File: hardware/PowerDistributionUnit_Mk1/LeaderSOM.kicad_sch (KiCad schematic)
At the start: 14 parts, among them J10 Logic Analyzer, J11 Logic Analyzer, J12 Logic Analyzer, U1 LeaderSOM

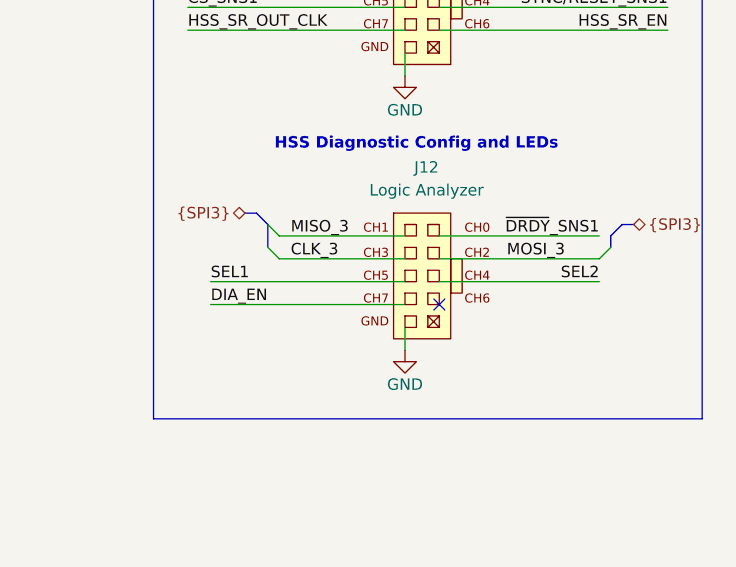
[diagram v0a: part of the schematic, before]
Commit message: add routing for DIA and HSS SR connections
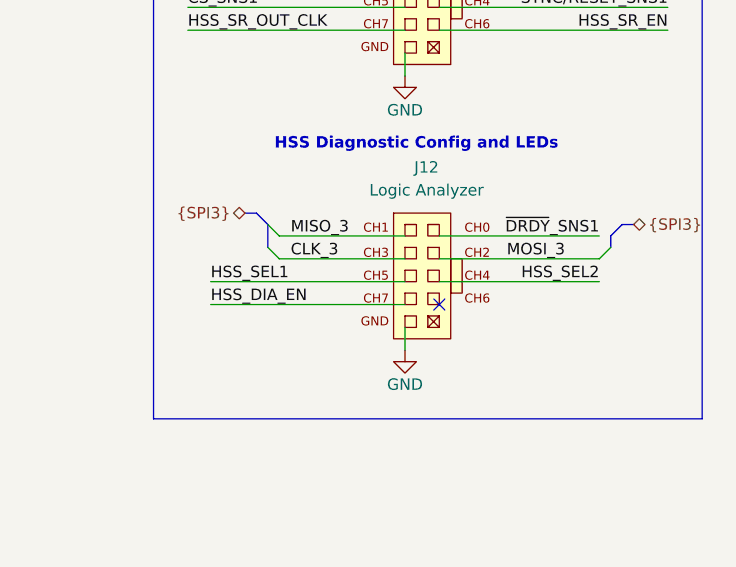
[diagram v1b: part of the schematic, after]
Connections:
- net DIA_EN is gone; now on net HSS_DIA_EN: J12.3 (CH7)
- net SEL1 is gone; now on net HSS_SEL1: J12.5 (CH5)
- net SEL2 is gone; now on net HSS_SEL2: J12.6 (CH4)
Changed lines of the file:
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@@
 		)
 	)
-	(label "SEL1"
+	(label "HSS_SEL1"
 		(at 218.44 113.03 0)
 		(effects
@@
 		)
 	)
-	(label "SEL2"
+	(label "HSS_SEL2"
 		(at 261.62 113.03 180)
 		(effects
@@
 		)
 	)
-	(label "DIA_EN"
+	(label "HSS_DIA_EN"
 		(at 218.44 115.57 0)
 		(effects

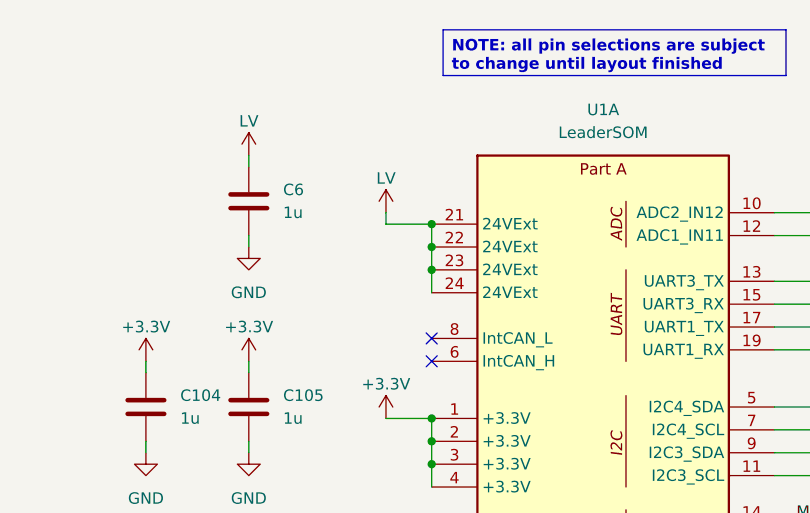
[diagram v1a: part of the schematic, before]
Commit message: all connections routed
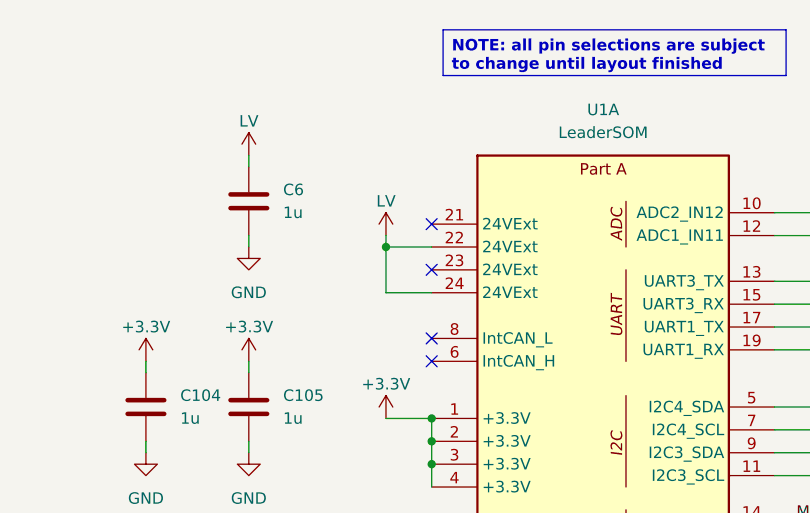
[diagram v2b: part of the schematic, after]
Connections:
- net LV: no longer U1.21 (24VExt), U1.23 (24VExt)
- no-connect marks 5 -> 7
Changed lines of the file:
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@@
 	)
 	(junction
-		(at 119.38 50.8)
+		(at 114.3 48.26)
 		(diameter 0)
 		(color 0 0 0 0)
@@
 	)
 	(junction
-		(at 119.38 48.26)
-		(diameter 0)
-		(color 0 0 0 0)
-	)
-	(junction
-		(at 119.38 45.72)
-		(diameter 0)
-		(color 0 0 0 0)
-	)
-	(junction
 		(at 119.38 69.85)
 		(diameter 0)
@@
 	)
 	(no_connect
+		(at 119.38 50.8)
+	)
+	(no_connect
+		(at 119.38 45.72)
+	)
+	(no_connect
 		(at 45.72 132.08)
 	)
@@
 	(wire
 		(pts
-			(xy 119.38 45.72) (xy 119.38 48.26)
-		)
-		(stroke
-			(width 0)
-			(type default)
-		)
-	)
-	(wire
-		(pts
 			(xy 55.88 142.24) (xy 55.88 143.51)
 		)
@@
 	(wire
 		(pts
-			(xy 226.06 107.95) (xy 240.03 107.95)
+			(xy 114.3 46.99) (xy 114.3 48.26)
 		)
 		(stroke
@@
 	(wire
 		(pts
-			(xy 157.48 146.05) (xy 167.64 146.05)
+			(xy 226.06 107.95) (xy 240.03 107.95)
 		)
 		(stroke
@@
 	(wire
 		(pts
-			(xy 157.48 125.73) (xy 165.1 125.73)
+			(xy 157.48 146.05) (xy 167.64 146.05)
 		)
 		(stroke
@@
 	(wire
 		(pts
-			(xy 226.06 77.47) (xy 240.03 77.47)
+			(xy 157.48 125.73) (xy 165.1 125.73)
 		)
 		(stroke
@@
 	(wire
 		(pts
-			(xy 87.63 69.85) (xy 87.63 71.12)
+			(xy 226.06 77.47) (xy 240.03 77.47)
 		)
 		(stroke
@@
 		)
 	)
-	(bus
+	(wire
 		(pts
-			(xy 168.91 77.47) (xy 170.18 76.2)
+			(xy 87.63 69.85) (xy 87.63 71.12)
 		)
 		(stroke
@@
 		)
 	)
-	(wire
+	(bus
 		(pts
-			(xy 119.38 50.8) (xy 119.38 53.34)
+			(xy 168.91 77.47) (xy 170.18 76.2)
 		)
 		(stroke
@@
 		)
 	)
-	(wire
+	(bus
 		(pts
-			(xy 119.38 48.26) (xy 119.38 50.8)
+			(xy 265.43 106.68) (xy 264.16 106.68)
 		)
 		(stroke
@@
 		)
 	)
-	(bus
+	(wire
 		(pts
-			(xy 265.43 106.68) (xy 264.16 106.68)
+			(xy 116.84 144.78) (xy 116.84 147.32)
 		)
 		(stroke
@@
 	(wire
 		(pts
-			(xy 116.84 144.78) (xy 116.84 147.32)
+			(xy 215.9 54.61) (xy 240.03 54.61)
 		)
 		(stroke
@@
 	(wire
 		(pts
-			(xy 215.9 54.61) (xy 240.03 54.61)
+			(xy 114.3 53.34) (xy 119.38 53.34)
 		)
 		(stroke
@@
 	(wire
 		(pts
+			(xy 114.3 48.26) (xy 114.3 53.34)
+		)
+		(stroke
+			(width 0)
+			(type default)
+		)
+	)
+	(wire
+		(pts
 			(xy 240.03 118.11) (xy 240.03 120.65)
 		)
@@
 	(wire
 		(pts
-			(xy 114.3 44.45) (xy 114.3 45.72)
-		)
-		(stroke
-			(width 0)
-			(type default)
-		)
-	)
-	(wire
-		(pts
 			(xy 243.84 77.47) (xy 260.35 77.47)
 		)
@@
 	(wire
 		(pts
-			(xy 114.3 45.72) (xy 119.38 45.72)
+			(xy 114.3 48.26) (xy 119.38 48.26)
 		)
 		(stroke
@@
 	(symbol
 		(lib_id "power:+24V")
-		(at 114.3 44.45 0)
+		(at 114.3 46.99 0)
 		(unit 1)
 		(exclude_from_sim no)
@@
 		(dnp no)
 		(property "Reference" "#PWR017"
-			(at 114.3 48.26 0)
+			(at 114.3 50.8 0)
 			(effects
 				(font
@@
 		)
 		(property "Value" "LV"
-			(at 114.3 40.64 0)
+			(at 114.3 43.18 0)
 			(effects
 				(font
@@
 		)
 		(property "Footprint" ""
-			(at 114.3 44.45 0)
+			(at 114.3 46.99 0)
 			(effects
 				(font
@@
 		)
 		(property "Datasheet" ""
-			(at 114.3 44.45 0)
+			(at 114.3 46.99 0)
 			(effects
 				(font
@@
 		)
 		(property "Description" "Power symbol creates a global label with name \"+24V\""
-			(at 114.3 44.45 0)
+			(at 114.3 46.99 0)
 			(effects
 				(font

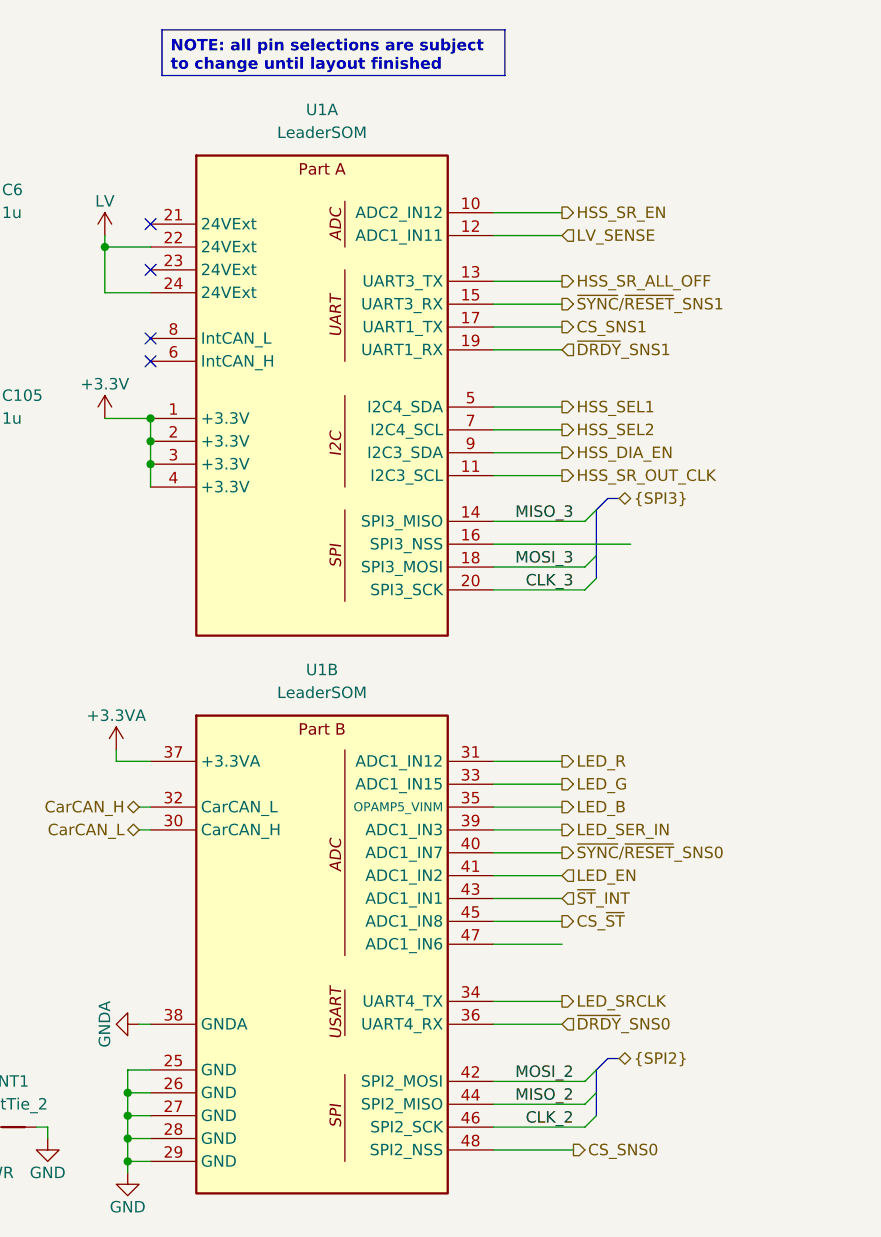
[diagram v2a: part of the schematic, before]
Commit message: update LeaderSOM symbol and SPI pinout (bottom) - need to swap SPI2 and SPI3 names, remove local library copy of LeaderSOM symbol
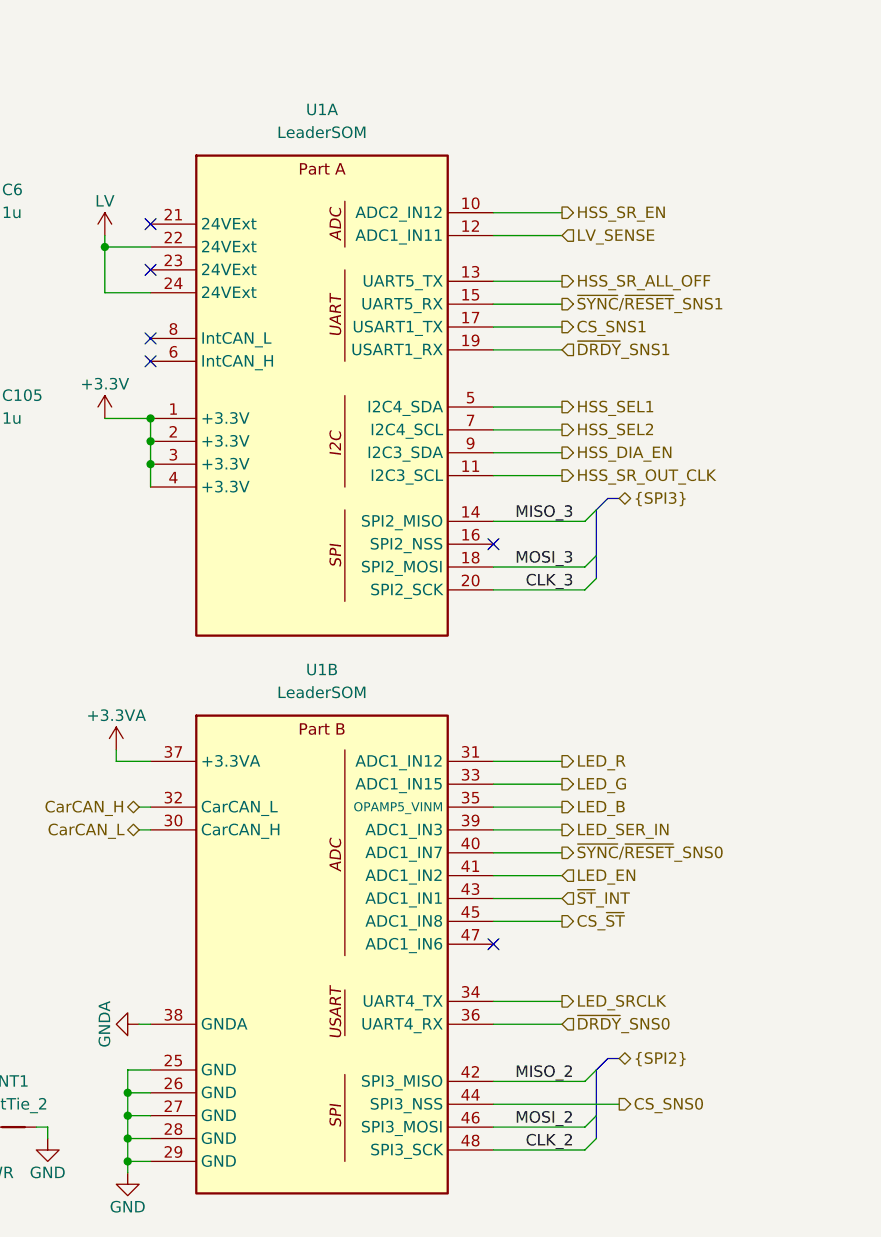
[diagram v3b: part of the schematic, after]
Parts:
- U1: footprint PowerDistributionUnitLib:LeaderSOM_Standoff -> UTSVT_Special:LeaderSOM; symbol PowerDistributionUnitLib:LeaderSOMConnector -> utsvt_connectors:LeaderSOMConnector
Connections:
- net CLK_2: now also U1.48 (SPI3_SCK); no longer U1.46 (SPI2_SCK)
- net CS_SNS0: now also U1.44 (SPI3_NSS); no longer U1.48 (SPI2_NSS)
- net MISO_2: now also U1.42 (SPI3_MISO); no longer U1.44 (SPI2_MISO)
- net MOSI_2: now also U1.46 (SPI3_MOSI); no longer U1.42 (SPI2_MOSI)
- no-connect marks 7 -> 9
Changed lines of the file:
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@@
 		)
 	)
-	(text_box "NOTE: all pin selections are subject to change until layout finished"
-		(exclude_from_sim no)
-		(at 120.65 24.13 0)
-		(size 38.1 5.08)
-		(margins 0.9525 0.9525 0.9525 0.9525)
-		(stroke
-			(width 0)
-			(type solid)
-			(color 255 0 0 1)
-		)
-		(fill
-			(type none)
-		)
-		(effects
-			(font
-				(size 1.27 1.27)
-				(thickness 0.254)
-				(bold yes)
-				(color 255 0 0 1)
-			)
-			(justify left top)
-		)
-	)
 	(text_box "LV is global... but this is pretty on the outside sheet."
 		(exclude_from_sim no)
@@
 	)
 	(no_connect
+		(at 157.48 125.73)
+	)
+	(no_connect
 		(at 119.38 45.72)
 	)
@@
 		(at 243.84 115.57)
 	)
+	(no_connect
+		(at 157.48 81.28)
+	)
 	(bus_entry
 		(at 224.79 78.74)
@@
 	)
 	(bus_entry
-		(at 168.91 142.24)
-		(size -1.27 1.27)
-		(stroke
-			(width 0)
-			(type default)
-		)
-	)
-	(bus_entry
 		(at 260.35 48.26)
 		(size -1.27 1.27)
@@
 	)
 	(bus_entry
+		(at 168.91 147.32)
+		(size -1.27 1.27)
+		(stroke
+			(width 0)
+			(type default)
+		)
+	)
+	(bus_entry
 		(at 224.79 76.2)
 		(size 1.27 1.27)
@@
 	(wire
 		(pts
-			(xy 157.48 143.51) (xy 167.64 143.51)
+			(xy 157.48 143.51) (xy 171.45 143.51)
 		)
 		(stroke
@@
 		)
 	)
-	(wire
+	(bus
 		(pts
-			(xy 157.48 81.28) (xy 172.72 81.28)
+			(xy 224.79 106.68) (xy 224.79 109.22)
 		)
 		(stroke
@@
 	(bus
 		(pts
-			(xy 224.79 106.68) (xy 224.79 109.22)
+			(xy 168.91 144.78) (xy 168.91 147.32)
 		)
 		(stroke
@@
 	(wire
 		(pts
-			(xy 157.48 125.73) (xy 165.1 125.73)
-		)
-		(stroke
-			(width 0)
-			(type default)
-		)
-	)
-	(wire
-		(pts
 			(xy 226.06 77.47) (xy 240.03 77.47)
 		)
@@
 	(wire
 		(pts
-			(xy 157.48 148.59) (xy 166.37 148.59)
-		)
-		(stroke
-			(width 0)
-			(type default)
-		)
-	)
-	(wire
-		(pts
 			(xy 226.06 110.49) (xy 240.03 110.49)
 		)
@@
 	(bus
 		(pts
-			(xy 168.91 142.24) (xy 168.91 144.78)
+			(xy 168.91 139.7) (xy 168.91 144.78)
 		)
 		(stroke
@@
 	(wire
 		(pts
+			(xy 157.48 148.59) (xy 167.64 148.59)
+		)
+		(stroke
+			(width 0)
+			(type default)
+		)
+	)
+	(wire
+		(pts
 			(xy 252.73 45.72) (xy 251.46 46.99)
 		)
@@
 		)
 	)
-	(bus
-		(pts
-			(xy 168.91 139.7) (xy 168.91 142.24)
-		)
-		(stroke
-			(width 0)
-			(type default)
-		)
-	)
 	(wire
 		(pts
@@
 	)
 	(label "MOSI_2"
-		(at 166.37 140.97 180)
+		(at 166.37 146.05 180)
 		(effects
 			(font
@@
 	)
 	(label "MISO_2"
-		(at 166.37 143.51 180)
+		(at 166.37 140.97 180)
 		(effects
 			(font
@@
 		)
 	)
-	(label "MOSI_3"
-		(at 260.35 77.47 180)
+	(label "CLK_2"
+		(at 166.37 148.59 180)
 		(effects
 			(font
@@
 		)
 	)
-	(label "~{SYNC}{slash}~{RESET}_SNS1"
-		(at 269.24 82.55 180)
+	(label "MOSI_3"
+		(at 260.35 77.47 180)
 		(effects
 			(font
@@
 		)
 	)
-	(label "CLK_2"
-		(at 166.37 146.05 180)
+	(label "~{SYNC}{slash}~{RESET}_SNS1"
+		(at 269.24 82.55 180)
 		(effects
 			(font
@@
 	(hierarchical_label "CS_SNS0"
 		(shape output)
-		(at 166.37 148.59 0)
+		(at 171.45 143.51 0)
 		(effects
 			(font
@@
 	)
 	(symbol
-		(lib_id "PowerDistributionUnitLib:LeaderSOMConnector")
+		(lib_id "utsvt_connectors:LeaderSOMConnector")
 		(at 138.43 64.77 0)
 		(unit 1)
@@
 			)
 		)
-		(property "Footprint" "PowerDistributionUnitLib:LeaderSOM_Standoff"
+		(property "Footprint" "UTSVT_Special:LeaderSOM"
 			(at 138.43 64.77 0)
 			(effects
@@
 	)
 	(symbol
-		(lib_id "PowerDistributionUnitLib:LeaderSOMConnector")
+		(lib_id "utsvt_connectors:LeaderSOMConnector")
 		(at 138.43 127 0)
 		(unit 2)
@@
 			)
 		)
-		(property "Footprint" "PowerDistributionUnitLib:LeaderSOM_Standoff"
+		(property "Footprint" "UTSVT_Special:LeaderSOM"
 			(at 138.43 127 0)
 			(effects

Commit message: change LSOM footprint to centered LSOM footprint, make centered LSOM footprint plated to address hidden pins on LSOM symbol
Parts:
- U1: footprint UTSVT_Special:LeaderSOM -> PowerDistributionUnitLib:LeaderSOM_Centered
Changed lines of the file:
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@@
 			)
 		)
-		(property "Footprint" "UTSVT_Special:LeaderSOM"
+		(property "Footprint" "PowerDistributionUnitLib:LeaderSOM_Centered"
 			(at 138.43 64.77 0)
 			(effects
@@
 			)
 		)
-		(property "Footprint" "UTSVT_Special:LeaderSOM"
+		(property "Footprint" "PowerDistributionUnitLib:LeaderSOM_Centered"
 			(at 138.43 127 0)
 			(effects

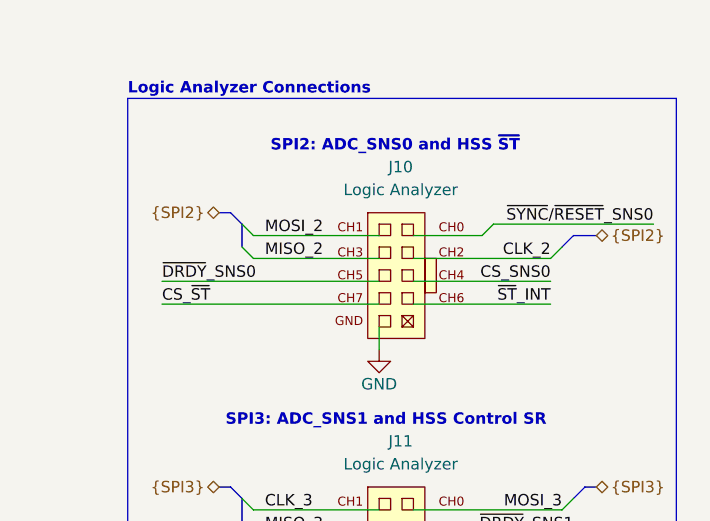
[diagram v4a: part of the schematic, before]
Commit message: reroute LSOM SPI connections, repin logic analyzer connections
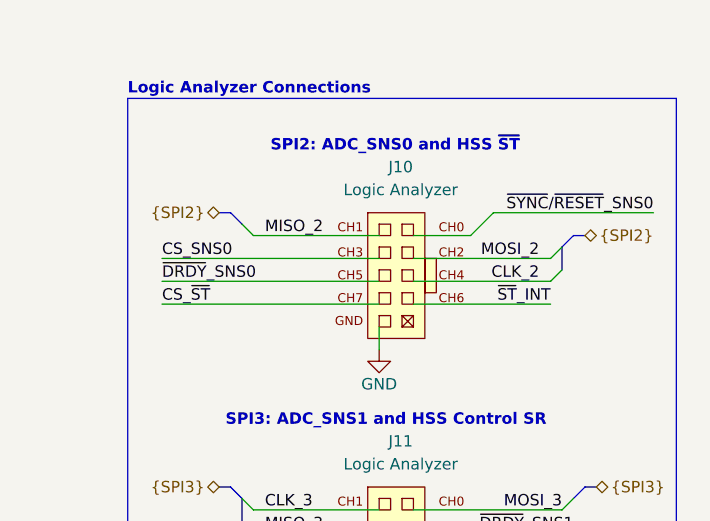
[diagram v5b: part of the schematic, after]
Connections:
- net CLK_2: now also J10.6 (CH4); no longer J10.8 (CH2)
- net CS_SNS0: now also J10.7 (CH3); no longer J10.6 (CH4)
- net MISO_2: now also J10.9 (CH1); no longer J10.7 (CH3)
- net MOSI_2: now also J10.8 (CH2); no longer J10.9 (CH1)

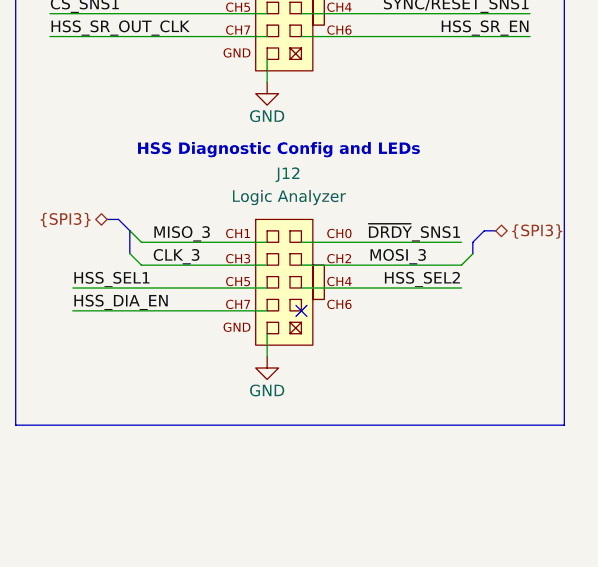
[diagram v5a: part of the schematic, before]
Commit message: add SRCLK_ENed connection to logic analyzer connector
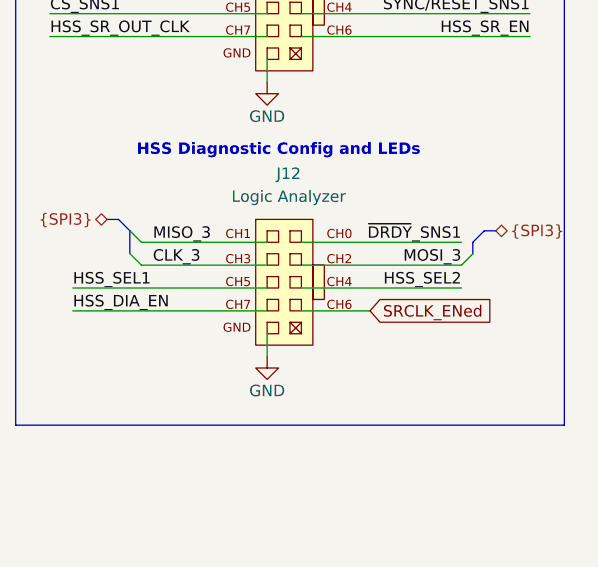
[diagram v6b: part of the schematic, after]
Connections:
- net SRCLK_ENed: now reaches J12.4 (CH6)
- no-connect marks 9 -> 8
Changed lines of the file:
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@@
-	)
-	(no_connect
-		(at 243.84 115.57)
 	)
 	(no_connect
@@
 	(wire
 		(pts
+			(xy 243.84 115.57) (xy 251.46 115.57)
+		)
+		(stroke
+			(width 0)
+			(type default)
+		)
+	)
+	(wire
+		(pts
 			(xy 100.33 146.05) (xy 101.6 146.05)
 		)
@@
 	)
 	(label "MOSI_3"
-		(at 257.81 110.49 180)
+		(at 261.62 110.49 180)
 		(effects
 			(font
@@
 		)
 	)
+	(global_label "SRCLK_ENed"
+		(shape input)
+		(at 251.46 115.57 0)
+		(fields_autoplaced yes)
+		(effects
+			(font
+				(size 1.27 1.27)
+			)
+			(justify left)
+		)
+		(property "Intersheetrefs" "${INTERSHEET_REFS}"
+			(at 266.1775 115.57 0)
+			(effects
+				(font
+					(size 1.27 1.27)
+				)
+				(justify left)
+				(hide yes)
+			)
+		)
+	)
